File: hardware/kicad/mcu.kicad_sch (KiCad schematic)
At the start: 10 parts, among them U1 ESP32-S3-MINI-1-N4R2

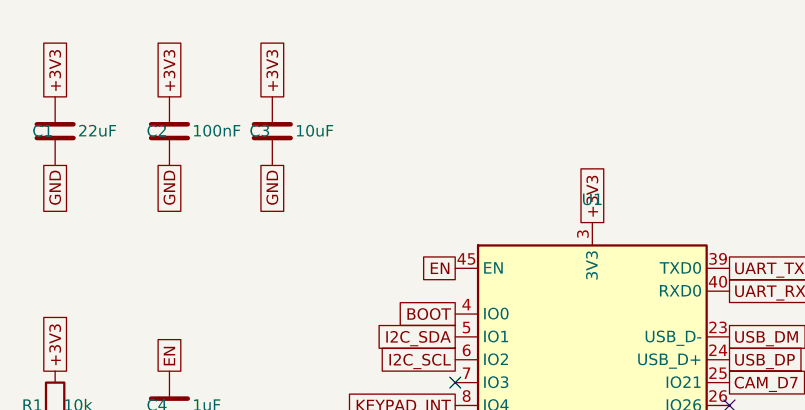
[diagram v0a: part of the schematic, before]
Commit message: Roadmap: $2,000 budget plan and $225 + $15/month pricing
Adds a money section to the launch roadmap: how the starting budget is
split into two supply waves, profit per unit and per subscriber, and how
preorders compound into bigger batches. Also saves the PR description.

Co-Authored-By: Claude Opus 5.5 <noreply@anthropic.com>
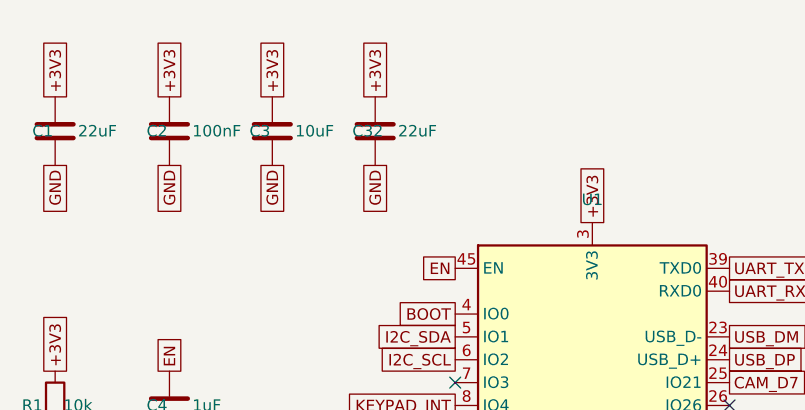
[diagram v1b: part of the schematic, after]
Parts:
- added C32: 22uF, Capacitor_SMD:C_0805_2012Metric, symbol Device:C
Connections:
- net +3V3: now also C32.1
- net GND: now also C32.2
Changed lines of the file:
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@@
 		(at 134.62 120.65)
+	)
+	(symbol
+		(lib_id "Device:C")
+		(at 95.25 59.69 0)
+		(unit 1)
+		(body_style 1)
+		(exclude_from_sim no)
+		(in_bom yes)
+		(on_board yes)
+		(in_pos_files yes)
+		(dnp no)
+		(property "Reference" "C32"
+			(at 92.71 59.69 0)
+			(show_name no)
+			(do_not_autoplace no)
+			(effects
+				(font
+					(size 1.27 1.27)
+				)
+				(justify left)
+			)
+		)
+		(property "Value" "22uF"
+			(at 97.79 59.69 0)
+			(show_name no)
+			(do_not_autoplace no)
+			(effects
+				(font
+					(size 1.27 1.27)
+				)
+				(justify left)
+			)
+		)
+		(property "Footprint" "Capacitor_SMD:C_0805_2012Metric"
+			(at 96.22 55.88 0)
+			(hide yes)
+			(show_name no)
+			(do_not_autoplace no)
+			(effects
+				(font
+					(size 1.27 1.27)
+				)
+			)
+		)
+		(property "Datasheet" ""
+			(at 95.25 59.69 0)
+			(hide yes)
+			(show_name no)
+			(do_not_autoplace no)
+			(effects
+				(font
+					(size 1.27 1.27)
+				)
+			)
+		)
+		(property "Description" "Unpolarized capacitor"
+			(at 95.25 59.69 0)
+			(hide yes)
+			(show_name no)
+			(do_not_autoplace no)
+			(effects
+				(font
+					(size 1.27 1.27)
+				)
+			)
+		)
+		(property "LCSC" "C45783"
+			(at 95.25 59.69 0)
+			(hide yes)
+			(show_name no)
+			(do_not_autoplace no)
+			(effects
+				(font
+					(size 1.27 1.27)
+				)
+			)
+		)
+		(pin "1"
+		)
+		(pin "2"
+		)
+		(instances
+			(project "ai_calc"
+				(path "/c7949ef3-e92b-45dc-b599-4b69606d677f/efb4cc23-340b-49a4-9ae6-5925a12f1a63"
+					(reference "C32")
+					(unit 1)
+				)
+			)
+		)
+	)
+	(global_label "+3V3"
+		(at 95.25 55.88 90)
+		(effects
+			(font
+				(size 1.27 1.27)
+			)
+			(justify left)
+		)
+	)
+	(global_label "GND"
+		(at 95.25 63.50 270)
+		(effects
+			(font
+				(size 1.27 1.27)
+			)
+			(justify right)
+		)
 	)
 	(sheet_instances

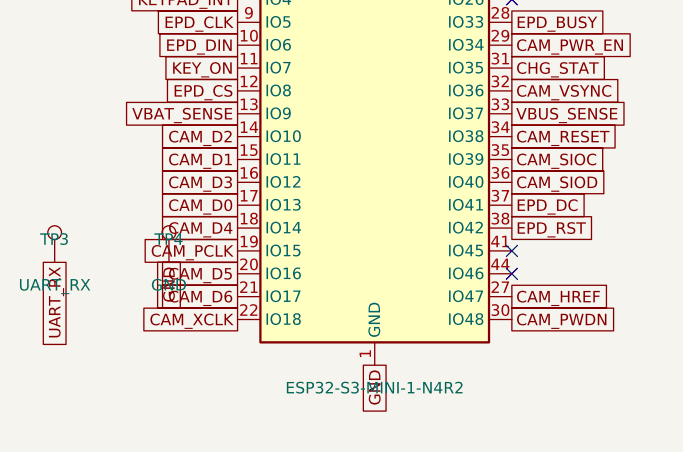
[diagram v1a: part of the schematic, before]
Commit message: PCB stage 11 finished (DRC 0/0/0) and unbranded fx-115ES replica CAD
Board: e-paper block moved 3.57 mm up to the measured LCD window and
fully re-routed; review fixes applied (R20 pull-up to VBUS_SENSE,
U3 -> RT9080-33GJ5 for longer standby, D7 orientation checked, 22 uF
bulk cap C32); test points TP5-TP7; locating-post holes 4.2 mm; antenna
keep-out strip; straightened track chains. DRC with refilled zones and
schematic parity: 0 errors, 0 unconnected, 0 parity issues. fab/,
fit-check and summary regenerated.

CAD: build_fx115es_replica.py builds an unbranded fx-115ES shell in
Fusion from the caliper readings and the 23 shell photos (60 bodies,
0 interferences), with F3D/STEP/STL exports and renders.

Open questions for Nirav are collected in hardware/QUESTIONS_AND_ISSUES.md.

Co-Authored-By: Claude Opus 5.5 <noreply@anthropic.com>
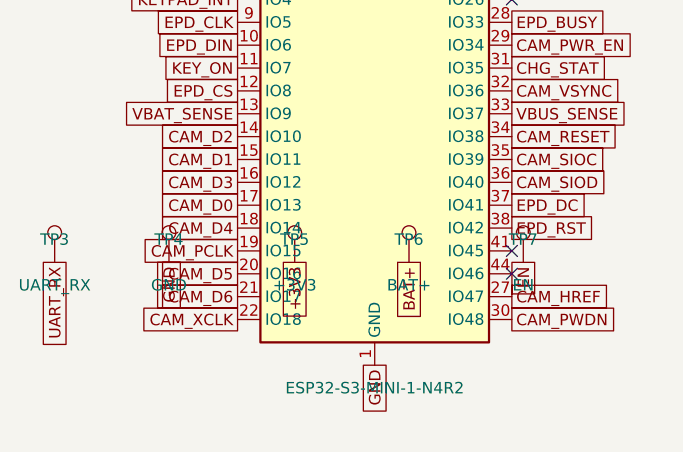
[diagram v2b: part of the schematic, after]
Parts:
- added TP5: +3V3, TestPoint:TestPoint_Pad_D1.5mm, symbol Connector:TestPoint
- added TP6: BAT+, TestPoint:TestPoint_Pad_D1.5mm, symbol Connector:TestPoint
- added TP7: EN, TestPoint:TestPoint_Pad_D1.5mm, symbol Connector:TestPoint
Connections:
- net +3V3: now also TP5.1
- net EN: now also TP7.1
- new net BAT+: TP6.1

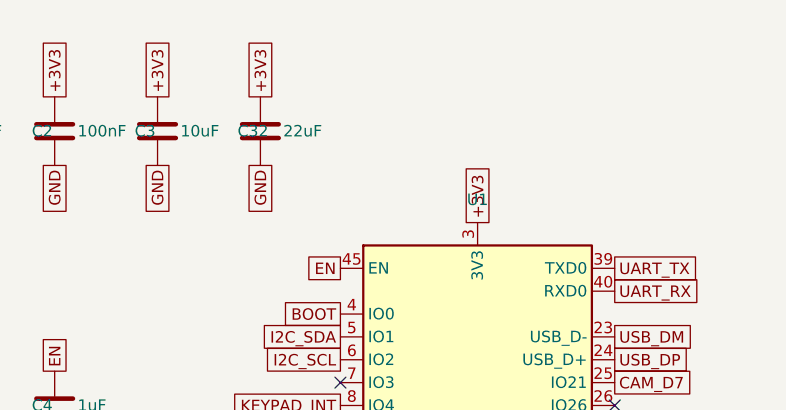
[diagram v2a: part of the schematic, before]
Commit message: Final review, v14 order prep, firmware fixes and production planning
- PCB v14 confirmed GO by final reviews (verification 06, 08, 11)
- CAD fit rev G with measured rib/pin/hook heights; grind zones 6, 6b, 6c
- Firmware: OTA updates, phone setup portal, low-battery gate, polish
- Docs: arrival checklist, vendor comparison, order walkthrough updates
- Production: QA test plan, knockoff shell plan, cost model

Co-Authored-By: Claude Opus 5.5 <noreply@anthropic.com>
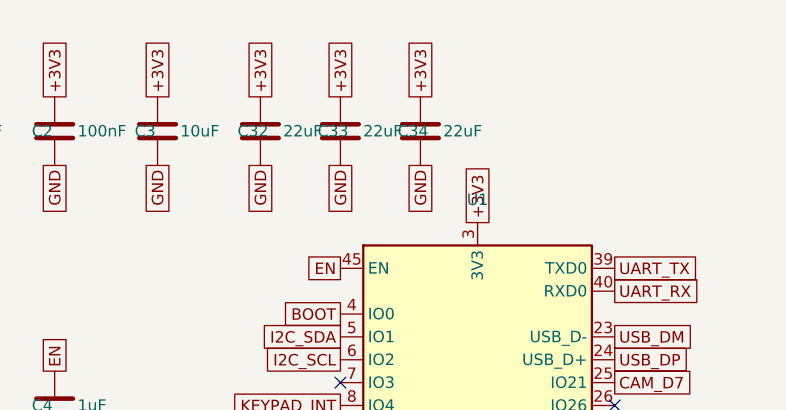
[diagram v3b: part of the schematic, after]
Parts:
- added C33, C34: 22uF, Capacitor_SMD:C_0805_2012Metric, symbol Device:C
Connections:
- net +3V3: now also C33.1, C34.1
- net GND: now also C33.2, C34.2
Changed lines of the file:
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@@
+		)
+	)
+	(symbol
+		(lib_id "Device:C")
+		(at 104.14 59.69 0)
+		(unit 1)
+		(body_style 1)
+		(exclude_from_sim no)
+		(in_bom yes)
+		(on_board yes)
+		(in_pos_files yes)
+		(dnp no)
+		(property "Reference" "C33"
+			(at 101.60 59.69 0)
+			(show_name no)
+			(do_not_autoplace no)
+			(effects
+				(font
+					(size 1.27 1.27)
+				)
+				(justify left)
+			)
+		)
+		(property "Value" "22uF"
+			(at 106.68 59.69 0)
+			(show_name no)
+			(do_not_autoplace no)
+			(effects
+				(font
+					(size 1.27 1.27)
+				)
+				(justify left)
+			)
+		)
+		(property "Footprint" "Capacitor_SMD:C_0805_2012Metric"
+			(at 105.11 55.88 0)
+			(hide yes)
+			(show_name no)
+			(do_not_autoplace no)
+			(effects
+				(font
+					(size 1.27 1.27)
+				)
+			)
+		)
+		(property "Datasheet" ""
+			(at 104.14 59.69 0)
+			(hide yes)
+			(show_name no)
+			(do_not_autoplace no)
+			(effects
+				(font
+					(size 1.27 1.27)
+				)
+			)
+		)
+		(property "Description" "Unpolarized capacitor"
+			(at 104.14 59.69 0)
+			(hide yes)
+			(show_name no)
+			(do_not_autoplace no)
+			(effects
+				(font
+					(size 1.27 1.27)
+				)
+			)
+		)
+		(property "LCSC" "C45783"
+			(at 104.14 59.69 0)
+			(hide yes)
+			(show_name no)
+			(do_not_autoplace no)
+			(effects
+				(font
+					(size 1.27 1.27)
+				)
+			)
+		)
+		(pin "1"
+		)
+		(pin "2"
+		)
+		(instances
+			(project "ai_calc"
+				(path "/c7949ef3-e92b-45dc-b599-4b69606d677f/efb4cc23-340b-49a4-9ae6-5925a12f1a63"
+					(reference "C33")
+					(unit 1)
+				)
+			)
+		)
+	)
+	(global_label "+3V3"
+		(at 104.14 55.88 90)
+		(effects
+			(font
+				(size 1.27 1.27)
+			)
+			(justify left)
+		)
+	)
+	(global_label "GND"
+		(at 104.14 63.50 270)
+		(effects
+			(font
+				(size 1.27 1.27)
+			)
+			(justify right)
+		)
+	)
+	(symbol
+		(lib_id "Device:C")
+		(at 113.03 59.69 0)
+		(unit 1)
+		(body_style 1)
+		(exclude_from_sim no)
+		(in_bom yes)
+		(on_board yes)
+		(in_pos_files yes)
+		(dnp no)
+		(property "Reference" "C34"
+			(at 110.49 59.69 0)
+			(show_name no)
+			(do_not_autoplace no)
+			(effects
+				(font
+					(size 1.27 1.27)
+				)
+				(justify left)
+			)
+		)
+		(property "Value" "22uF"
+			(at 115.57 59.69 0)
+			(show_name no)
+			(do_not_autoplace no)
+			(effects
+				(font
+					(size 1.27 1.27)
+				)
+				(justify left)
+			)
+		)
+		(property "Footprint" "Capacitor_SMD:C_0805_2012Metric"
+			(at 114.00 55.88 0)
+			(hide yes)
+			(show_name no)
+			(do_not_autoplace no)
+			(effects
+				(font
+					(size 1.27 1.27)
+				)
+			)
+		)
+		(property "Datasheet" ""
+			(at 113.03 59.69 0)
+			(hide yes)
+			(show_name no)
+			(do_not_autoplace no)
+			(effects
+				(font
+					(size 1.27 1.27)
+				)
+			)
+		)
+		(property "Description" "Unpolarized capacitor"
+			(at 113.03 59.69 0)
+			(hide yes)
+			(show_name no)
+			(do_not_autoplace no)
+			(effects
+				(font
+					(size 1.27 1.27)
+				)
+			)
+		)
+		(property "LCSC" "C45783"
+			(at 113.03 59.69 0)
+			(hide yes)
+			(show_name no)
+			(do_not_autoplace no)
+			(effects
+				(font
+					(size 1.27 1.27)
+				)
+			)
+		)
+		(pin "1"
+		)
+		(pin "2"
+		)
+		(instances
+			(project "ai_calc"
+				(path "/c7949ef3-e92b-45dc-b599-4b69606d677f/efb4cc23-340b-49a4-9ae6-5925a12f1a63"
+					(reference "C34")
+					(unit 1)
+				)
+			)
+		)
+	)
+	(global_label "+3V3"
+		(at 113.03 55.88 90)
+		(effects
+			(font
+				(size 1.27 1.27)
+			)
+			(justify left)
+		)
+	)
+	(global_label "GND"
+		(at 113.03 63.50 270)
+		(effects
+			(font
+				(size 1.27 1.27)
+			)
+			(justify right)
 		)
 	)
